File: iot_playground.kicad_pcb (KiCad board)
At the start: 2 copper layers, 111 parts, among them J101 Micro_SD_Card_Det_Hirose_DM3C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, J102 Conn_01x04, J103 Conn_01x04, J104 Conn_01x08, J105 Conn_01x02, J201 USB_C_Receptacle_USB2.0, J701 Conn_01x08, J702 Conn_01x08, Q201 Q_NMOS_GSD, Q301 S8050, Q302 S8050, Q501 Q_PMOS_DGS, Q502 FS8205, SW101 SW_SPST, SW102 SW_SPST, U101 LIS2DW12, U102 ESP32-WROOM-32E, U103 SHT30-DIS-B2.5KS, U104 LTR-F216A, U105 UHE4913, U106 PCF8563T, U301 CP2102-GMR, U401 XC6220B331MR-G, U402 MT3608L, U501 FS312F-G, U502 TP4056, U503 MAX17048, U601 SN74AHCT1G125DBVR, U701 PCA9535PW, Y101 32.768k

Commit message: update pcb
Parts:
- moved U701 115.9 mm to (63.8, 80.0)
- moved C701 112.3 mm to (62.7, 72.6)
- moved J101 85.9 mm to (165.6, 78.5)
- moved Q502 74.1 mm to (133.4, 64.2)
- moved U503 74.1 mm to (132.7, 68.2)
- moved R401 71.6 mm to (78.6, 123.9)
- moved R402 71.6 mm to (78.6, 126.8)
- moved R403 71.6 mm to (78.6, 129.8)
- moved C401 71.6 mm to (69.3, 123.7)
- moved C402 71.6 mm to (69.3, 126.2)
- moved C403 71.6 mm to (69.3, 128.7)
- moved C404 71.6 mm to (69.3, 131.2)
- moved LED501 67.5 mm to (132.9, 73.7)
- moved C101 63.3 mm to (186.0, 71.0)
- moved C102 63.3 mm to (186.0, 73.5)
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
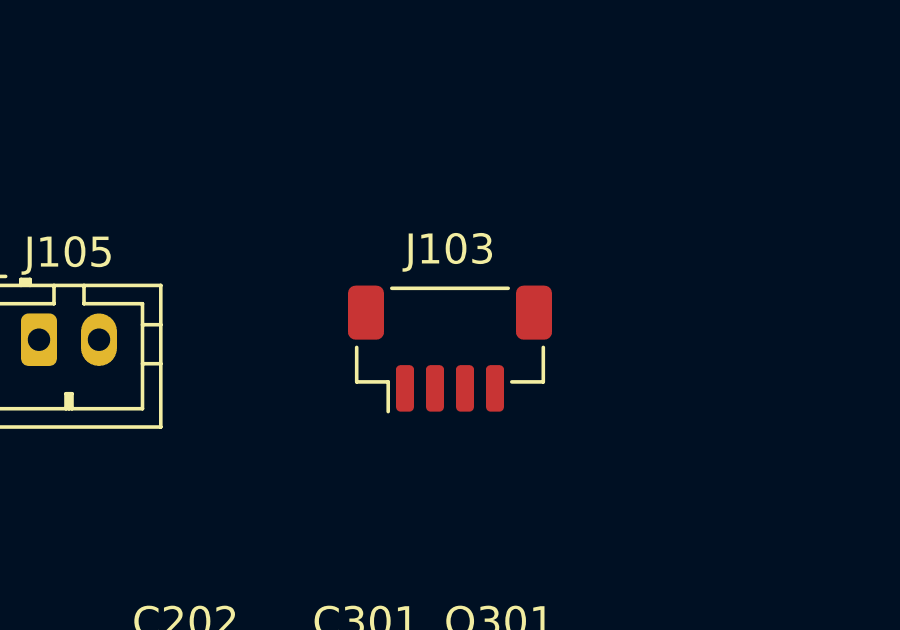
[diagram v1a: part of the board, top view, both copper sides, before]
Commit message: update 3d models
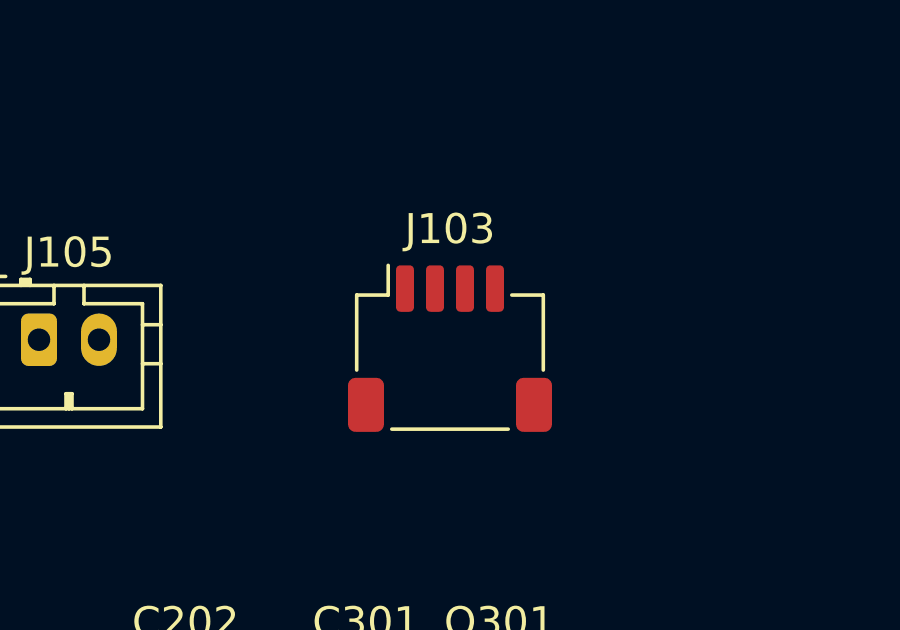
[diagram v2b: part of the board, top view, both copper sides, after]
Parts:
- J103: footprint Connector_JST:JST_SH_BM04B-SRSS-TB_1x04-1MP_P1.00mm_Vertical -> Connector_JST:JST_SH_SM04B-SRSS-TB_1x04-1MP_P1.00mm_Horizontal

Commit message: update layout
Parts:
- added C115: 100nF, Capacitor_SMD:C_0603_1608Metric, F.Cu at (101.0, 77.2)
- added C116: 100nF, Capacitor_SMD:C_0603_1608Metric, F.Cu at (100.2, 128.9)
- added D202: SP0503BAHT, Package_TO_SOT_SMD:SOT-143, F.Cu at (105.7, 103.5)
- added H101: MountingHole_Pad, MountingHole:MountingHole_3.2mm_M3_Pad, F.Cu at (97.0, 135.0)
- added H102: MountingHole_Pad, MountingHole:MountingHole_3.2mm_M3_Pad, F.Cu at (185.0, 135.0)
- added H103: MountingHole_Pad, MountingHole:MountingHole_3.2mm_M3_Pad, F.Cu at (185.0, 67.0)
- added H104: MountingHole_Pad, MountingHole:MountingHole_3.2mm_M3_Pad, F.Cu at (97.0, 67.0)
- added J106: Conn_01x08, Connector_PinSocket_2.54mm:PinSocket_1x08_P2.54mm_Vertical, F.Cu at (178.1, 138.2)
- added J202: USB_C_Receptacle_USB2.0, User Custom Footprint:USB_C_Receptable_918-418K2023S40001, F.Cu at (96.7, 104.1)
- added R203: 5K1, Capacitor_SMD:C_0603_1608Metric, F.Cu at (93.7, 97.8)
- added R204: 5K1, Capacitor_SMD:C_0603_1608Metric, F.Cu at (97.1, 97.8)
- C103: value 100nF -> 1uF
- C108: value 22uF -> 10uF
- J105: footprint Connector_JST:JST_PH_B2B-PH-K_1x02_P2.00mm_Vertical -> Connector_JST:JST_PH_S2B-PH-K_1x02_P2.00mm_Horizontal
- locked: renamed from U102; value ESP32-WROOM-32E -> ESP32-S3-WROOM-1-N8R2; footprint RF_Module:ESP32-WROOM-32D -> User Custom Footprint:ESP32-S3-WROOM
- moved SW101 131.0 mm to (95.5, 75.3), turned to 180 degrees
- moved C101 128.6 mm to (57.4, 70.7)
- moved C102 128.6 mm to (57.4, 73.2)
- moved C103 128.6 mm to (57.4, 75.7)
- moved C104 128.6 mm to (57.4, 78.2)
- moved C105 128.6 mm to (57.4, 80.7)
- moved C107 128.6 mm to (57.4, 85.8)
- moved C108 128.6 mm to (61.4, 70.7)
- moved C109 128.6 mm to (61.4, 73.2)
- moved C110 128.6 mm to (61.4, 75.7)
- moved C111 128.6 mm to (61.4, 78.2)
- moved R101 128.6 mm to (61.4, 83.3)
- moved R102 128.6 mm to (61.4, 85.8)
- moved R103 128.6 mm to (65.4, 70.7)
- moved R104 128.6 mm to (65.4, 73.2)
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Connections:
- net Net-(D201-K-Pad4) renamed /USBC-2.0/USB_VCC
- C202 pad 1: VBUS -> +5V
- C302 pad 1: VBUS -> +5V
- C303 pad 1: VBUS -> +5V
- C503 pad 1: -BATT -> +BATT
- C504 pad 2: +BATT -> -BATT
- C505 pad 1: -BATT -> +BATT
- D502 pad 2: -BATT -> +BATT
- FB201 pad 2: VBUS -> +5V
- J104 pad 1: /IO2 -> +5V
- J104 pad 3: +5V -> GND
- J104 pad 4: GND -> /IO35
- J104 pad 5: GND -> /IO36
- J104 pad 6: /RTC_CLKO -> /IO37
- J104 pad 7: /IO34 -> /IO45
- J104 pad 8: /IO35 -> /RTC_CLKO
- J701 pad 1: /IO_Expander/P00 -> /IO_Expander/P07
- J701 pad 2: /IO_Expander/P01 -> /IO_Expander/P06
- J701 pad 3: /IO_Expander/P02 -> /IO_Expander/P05
- J701 pad 4: /IO_Expander/P03 -> /IO_Expander/P04
- J701 pad 5: /IO_Expander/P04 -> /IO_Expander/P03
- J701 pad 6: /IO_Expander/P05 -> /IO_Expander/P02
- J701 pad 7: /IO_Expander/P06 -> /IO_Expander/P01
- J701 pad 8: /IO_Expander/P07 -> /IO_Expander/P00
- J702 pad 1: /IO_Expander/P10 -> /IO_Expander/P17
- J702 pad 2: /IO_Expander/P11 -> /IO_Expander/P16
- J702 pad 3: /IO_Expander/P12 -> /IO_Expander/P15
- J702 pad 4: /IO_Expander/P13 -> /IO_Expander/P14
- J702 pad 5: /IO_Expander/P14 -> /IO_Expander/P13
- J702 pad 6: /IO_Expander/P15 -> /IO_Expander/P12
- J702 pad 7: /IO_Expander/P16 -> /IO_Expander/P11
- J702 pad 8: /IO_Expander/P17 -> /IO_Expander/P10
- LED501 pad 1: Net-(LED501-BK) -> unconnected-(LED501-BK-Pad1)
- LED501 pad 4: unconnected-(LED501-RK-Pad4) -> Net-(LED501-RK)
- Q201 pad 1: VBUS -> +5V
- Q502 pad 1: +BATT -> -BATT
- R502 pad 1: -BATT -> +BATT
- R506 pad 1: /Battery_Management/~{CHRG} -> /Battery_Management/~{STDBY}
- R507 pad 1: /Battery_Management/~{STDBY} -> /Battery_Management/~{CHRG}
- R507 pad 2: Net-(LED501-BK) -> Net-(LED501-RK)
- U301 pad 7: VBUS -> +5V
- U301 pad 8: VBUS -> +5V
- U501 pad 6: +BATT -> -BATT
- U502 pad 5: -BATT -> +BATT
- U503 pad 2: -BATT -> +BATT
- U503 pad 3: -BATT -> +BATT
- locked pad 10: /SD_DET -> /TXD1
- locked pad 11: /~{ALRT} -> /RXD1
- locked pad 12: /ACC_INT -> /IO8
- locked pad 13: /IO_INT -> /USB_N
- locked pad 14: /LED_IC -> /USB_P
- locked pad 15: GND -> /IO3
- locked pad 16: /~{BUF_EN} -> unconnected-(U102-*IO46-Pad16)
- locked pad 17: unconnected-(U102-SHD/SD2-Pad17) -> /~{SDA}
- locked pad 18: unconnected-(U102-SWP/SD3-Pad18) -> /~{SCL}
- locked pad 19: unconnected-(U102-SCS/CMD-Pad19) -> /SD_SS
- locked pad 20: unconnected-(U102-SCK/CLK-Pad20) -> /SD_SCK
- locked pad 21: unconnected-(U102-SDO/SD0-Pad21) -> /SD_MOSI
- locked pad 22: unconnected-(U102-SDI/SD1-Pad22) -> /SD_MISO
- locked pad 23: /HALL_SNSR -> /LED_IC
- locked pad 24: /IO2 -> /SD_DET
- locked pad 25: /IO0 -> /~{RTC_INT}
- locked pad 26: /PWR_FLG -> /IO45
- locked pad 27: /RXD1 -> /IO0
- locked pad 28: /TXD1 -> /IO35
- locked pad 29: /SD_SS -> /IO36
- locked pad 30: /SD_SCK -> /IO37
- locked pad 31: /SD_MISO -> /~{BUF_EN}
- locked pad 32: unconnected-(U102-NC-Pad32) -> /IO_INT
- locked pad 33: /~{SDA} -> /HALL_SNSR
- locked pad 34: /ESP_RX -> /ACC_INT
- locked pad 35: /ESP_TX -> /ALS_INT
- locked pad 36: /~{SCL} -> /ESP_RX
- locked pad 37: /SD_MOSI -> /ESP_TX
- locked pad 38: GND -> /IO2
- locked pad 39: GND -> /IO1
- locked pad 4: unconnected-(U102-SENSOR_VP-Pad4) -> /IO4
- locked pad 5: unconnected-(U102-SENSOR_VN-Pad5) -> /IO5
- locked pad 6: /IO34 -> /IO6
- locked pad 7: /IO35 -> /IO7
- locked pad 8: /ALS_INT -> /PWR_FLG
- locked pad 9: /~{RTC_INT} -> /~{ALRT}
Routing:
- net +5V: track 0.00 -> 101.1 mm, vias 0 -> 11
- net /USB_N: track 0.00 -> 86.3 mm
- net /USB_P: track 0.00 -> 84.4 mm
- net /IO4: track 0.00 -> 53.5 mm, vias 0 -> 1
- net /IO0: track 0.00 -> 37.8 mm, vias 0 -> 2
- net /USBC-2.0/USB_VCC: track 0.00 -> 31.1 mm, vias 0 -> 8
- net /IO2: track 0.00 -> 30.4 mm, vias 0 -> 1
- net /IO1: track 0.00 -> 29.9 mm, vias 0 -> 1
- net /CP2102-ESP32/D_P: track 0.00 -> 23.2 mm, vias 0 -> 2
- net /CP2102-ESP32/D_N: track 0.00 -> 22.6 mm
- net +BATT: track 0.00 -> 20.5 mm
- net -BATT: track 0.00 -> 16.5 mm
- net /CP2102-ESP32/DTR: track 0.00 -> 10.8 mm, vias 0 -> 2
- net Net-(J202-CC2): track 0.00 -> 10.5 mm
- net Net-(J201-CC1): track 0.00 -> 10.3 mm
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- added copper zone on In2.Cu, net +3V3
- added copper zone on F.Cu, net +5V
- added copper zone on In2.Cu, net +5V
- added copper zone on F.Cu, net /Battery_Management/VCC
- added copper zone on F.Cu, net /USBC-2.0/USB_VCC
- added copper zone on In2.Cu, net /USBC-2.0/USB_VCC
- added copper zone on B.Cu, net GND
- added copper zone on F.Cu, net GND
- added copper zone on In1.Cu, net GND
- added copper zone on F.Cu, net Net-(D401-A)
- added copper zone on F.Cu, net Net-(U402-FB)
- added copper zone on F.Cu, net Net-(U402-OC)
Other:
- board outline added: 100 x 80 mm
- copper layers 2 -> 4
- board text added: "+3V3"
- board text added: "+5V"
- board text added: "4.2V Lithium Battery"
- board text added: "5V TX RX G"
- board text added: "GND"
- board text added: "IO1"
- board text added: "IO2"
- board text added: "IO3"
- board text added: "IO35"
- board text added: "IO36"
- board text added: "IO37"
- board text added: "IO4"
- board text added: "IO45"
- board text added: "IO5"
- board text added: "IO6"
- board text added: "IO7"
- board text added: "IO8"
- board text added: "Nextion"
- board text added: "P10"
- board text added: "P11"
- board text added: "P12"
- board text added: "P13"
- board text added: "P14"
- board text added: "P15"
- board text added: "P16"
- board text added: "P17"
- board text added: "PO0"
- board text added: "PO1"
- board text added: "PO2"
- board text added: "PO3"
- board text added: "PO4"
- board text added: "PO5"
- board text added: "PO6"
- board text added: "PO7"
- board text added: "RTC CLK"

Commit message: update pcb layout
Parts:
- removed D502: D_Schottky, Diode_SMD:D_SMA
- moved R105 125.5 mm to (182.2, 121.7)
- moved R106 125.5 mm to (182.2, 124.2)
- moved C103 124.6 mm to (181.9, 81.9)
- moved C108 121.2 mm to (181.9, 84.5)
- moved C109 121.2 mm to (181.9, 87.0)
- moved R101 120.6 mm to (181.9, 89.5)
- moved C110 113.4 mm to (174.8, 77.4)
- moved C111 113.4 mm to (174.8, 79.9)
- moved R110 112.4 mm to (186.5, 84.9)
- moved C104 101.3 mm to (148.6, 122.4), turned to 90 degrees
- moved C105 98.8 mm to (146.9, 122.4), turned to 90 degrees
- moved R103 98.2 mm to (161.5, 91.1)
- moved R104 98.2 mm to (161.5, 93.6)
- moved C112 87.5 mm to (152.1, 114.8)
- moved R108 85.3 mm to (152.1, 117.3)
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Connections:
- Q501 pad 3: Net-(D502-K) -> +BATT
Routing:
- net /IO_Expander/P17: track 0.00 -> 24.5 mm
- net /IO_Expander/P00: track 0.00 -> 22.3 mm
- net /IO_Expander/P16: track 0.00 -> 21.3 mm
- net /IO_Expander/P01: track 0.00 -> 20.0 mm
- net /IO_Expander/P15: track 0.00 -> 18.7 mm
- net /IO_Expander/P02: track 0.00 -> 17.8 mm
- net /IO_Expander/P14: track 0.00 -> 15.8 mm
- net +3V3: track 1.81 -> 17.5 mm, vias 0 -> 3
- net /IO_Expander/P03: track 0.00 -> 15.6 mm
- net /IO_Expander/P04: track 0.00 -> 13.5 mm
- net /IO_Expander/P13: track 0.00 -> 13.4 mm
- net /IO_Expander/P05: track 0.00 -> 11.4 mm
- net /IO_Expander/P12: track 0.00 -> 11.4 mm
- net /IO_Expander/P07: track 0.00 -> 10.0 mm
- net /IO_Expander/P06: track 0.00 -> 9.34 mm
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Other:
- board text added: "5V RX TX G"
- board text removed: "5V TX RX G"

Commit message: update pcb design
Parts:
- moved R109 10.6 mm to (124.7, 131.4)
- moved LED501 5.06 mm to (111.5, 134.5), turned to 0 degrees
- moved R507 4.42 mm to (112.6, 137.8), turned to 90 degrees
- moved R107 4.06 mm to (132.6, 131.6), turned to 180 degrees
- moved R506 1.42 mm to (110.5, 137.8), turned to 90 degrees
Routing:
- net GND: track 9.73 -> 13.9 mm
- net +3V3: track 17.5 -> 19.1 mm, vias 3 -> 4
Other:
- board text added: "Lithium Battery - +"
- board text added: "Qwiic I^{2}C"
- board text removed: "4.2V Lithium Battery"
